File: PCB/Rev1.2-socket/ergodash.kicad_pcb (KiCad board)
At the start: 2 copper layers, 149.9 x 127.4 mm, 92 parts, among them J1 5PIN, M1 Speaker, SW1 SW_PUSH, SW10 SW_PUSH, SW11 SW_PUSH, SW12 SW_PUSH, SW13 SW_PUSH, SW14 SW_PUSH, SW15 SW_PUSH, SW16 SW_PUSH, SW17 SW_PUSH, SW18 SW_PUSH, SW19 SW_PUSH, SW2 SW_PUSH, SW20 SW_PUSH, SW21 SW_PUSH, SW22 SW_PUSH, SW23 SW_PUSH, SW24 SW_PUSH, SW25 SW_PUSH, SW26 SW_PUSH, SW27 SW_PUSH, SW28 SW_PUSH, SW29 SW_Push, SW3 SW_PUSH, SW30 SW_PUSH, SW31 SW_PUSH, SW32 SW_PUSH, SW33 SW_PUSH, SW34 SW_PUSH, SW35 SW_PUSH, SW36 SW_PUSH, SW37 SW_Push, SW38 SW_PUSH, SW39 SW_PUSH, SW4 SW_PUSH, SW40 SW_PUSH, SW41 SW_PUSH, SW5 SW_PUSH, SW6 SW_PUSH, SW7 SW_PUSH, SW8 SW_PUSH, SW9 SW_PUSH, U1 HOLE, U2 HOLE, U3 ProMicro, U4 HOLE, U5 HOLE, U7 HOLE, U8 HOLE, U9 HOLE

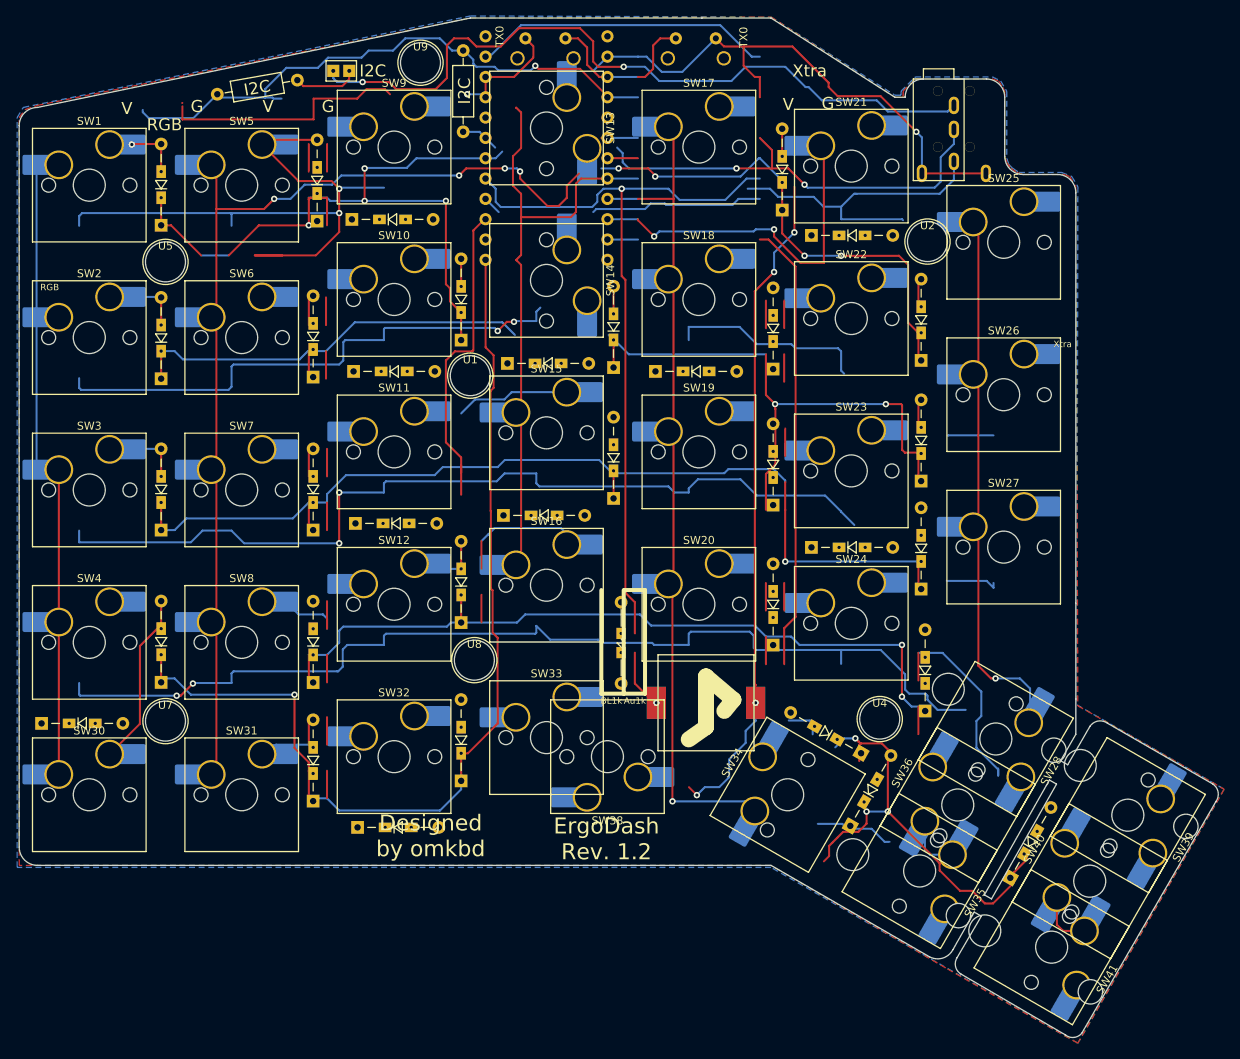
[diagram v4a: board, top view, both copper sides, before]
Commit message: Route the left board and drop alternative key layouts
Manual routing of the key matrix done in the GUI. Remove the
alternative-position switches (SW36, SW38, SW39, SW41) from the
schematic, keeping SW40 as the only 2U key, and delete the now
orphaned 2U stabilizer at the old SW36 position, which also
resolves the hole clearance conflict with the SW35 socket pad.
Re-apply the U6 on_board=no exclusion that was lost to a
concurrent eeschema save.

Co-Authored-By: Claude Fable 5 <noreply@anthropic.com>
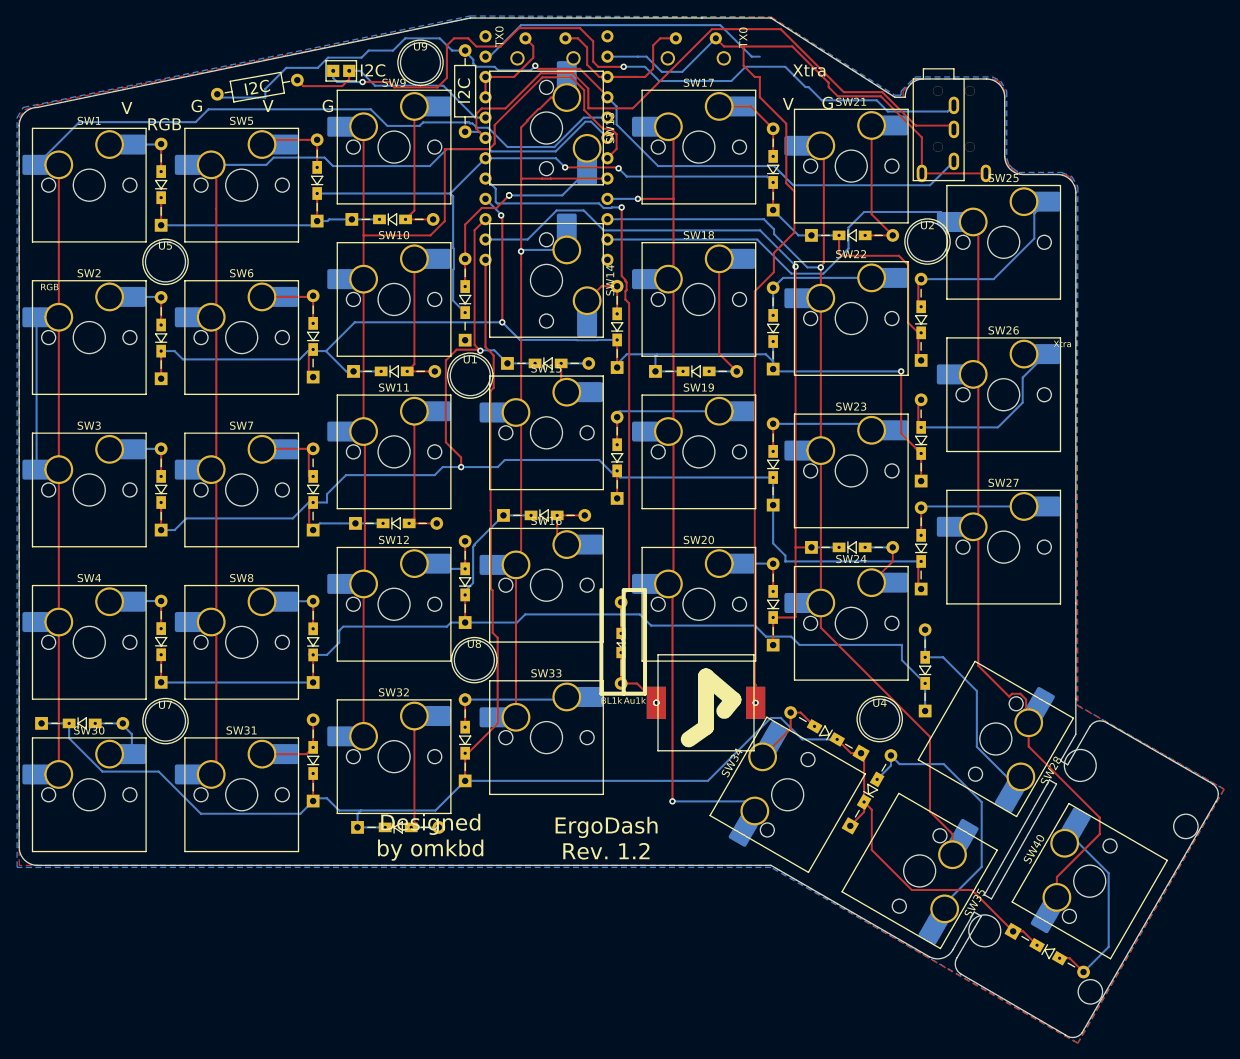
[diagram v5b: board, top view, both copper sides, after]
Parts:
- removed the ? at (195.6, 135.5)
- removed SW36, SW38, SW39, SW41: SW_PUSH, socket:SW_Hotswap_Kailh_MX_Plated
- moved D68 6.70 mm to (202.5, 151.3), turned to -30 degrees
- moved D17 1.13 mm to (172.5, 61.1)
- moved D13 0.50 mm to (134.0, 77.4)
- moved D12 0.50 mm to (134.0, 112.6)
- moved D32 0.50 mm to (134.0, 132.4)
- moved D14 0.45 mm to (153.0, 80.8)
- moved D19 0.45 mm to (153.0, 97.1)
- moved R2 0.25 mm to (134.0, 41.1)
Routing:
- net /col2: track 3.81 -> 130.9 mm
- net /col0: track 76.2 -> 173.3 mm
- net Net-(D18-A): track 112.7 -> 18.4 mm, vias 2 -> 0
- net /row1: track 246.0 -> 158.4 mm, vias 4 -> 3
- net /col5: track 52.7 -> 125.4 mm, vias 2 -> 1
- net Net-(D5-A): track 80.9 -> 10.6 mm, vias 2 -> 0
- net /col6: track 79.8 -> 146.1 mm, vias 1 -> 0
- net /row3: track 294.3 -> 231.8 mm, vias 4 -> 1
- net /row4: track 194.8 -> 235.9 mm, vias 4 -> 0
- net GND: track 198.4 -> 159.3 mm, vias 6 -> 1
- net Net-(D34-A): track 0.00 -> 32.7 mm
- net Net-(D68-A): track 0.00 -> 26.5 mm
- net /Audio: track 96.2 -> 73.7 mm
- net Net-(D13-A): track 3.45 -> 25.8 mm, vias 0 -> 2
- net Net-(D25-A): track 3.45 -> 24.9 mm
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
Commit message: Exclude SW37 (right-hand reset switch) from the left board
SW37 is the back-side reset switch used when the reversible board
served as the right half, so the left board does not need it.
Exclude it via on_board=no like U6 instead of moving it away from
the SW13 socket pad it overlapped. Also refill zones (clears stale
VCC fill under new row3 tracks) and document the thumb layout
decision in CLAUDE.md.

Co-Authored-By: Claude Fable 5 <noreply@anthropic.com>
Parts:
- removed SW37: SW_Push, library:tact_switch2
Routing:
- net /row0: track 148.4 -> 151.9 mm
- net /rst: track 24.6 -> 23.0 mm
- net GND: track 159.3 -> 157.9 mm
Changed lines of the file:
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@@
 		)
 	)
-	(footprint "library:tact_switch2"
-		(layer "B.Cu")
-		(at 144.018 39.624 180)
-		(property "Reference" "SW37"
-			(at 0 1.27 180)
-			(layer "Dwgs.User")
-			(hide yes)
-			(effects
-				(font
-					(size 1 1)
-					(thickness 0.15)
-				)
-			)
-		)
-		(property "Value" "SW_Push"
-			(at 0 -1.27 180)
-			(layer "B.Fab")
-			(effects
-				(font
-					(size 1 1)
-					(thickness 0.15)
-				)
-				(justify mirror)
-			)
-		)
-		(property "Datasheet" ""
-			(at 0 0 180)
-			(layer "F.Fab")
-			(hide yes)
-			(effects
-				(font
-					(size 1.27 1.27)
-				)
-			)
-		)
-		(property "Description" ""
-			(at 0 0 180)
-			(layer "F.Fab")
-			(hide yes)
-			(effects
-				(font
-					(size 1.27 1.27)
-				)
-			)
-		)
-		(sheetname "/")
-		(sheetfile "ergodash.kicad_sch")
-		(units
-			(unit
-				(name "A")
-				(pins "1" "2")
-			)
-		)
-		(attr through_hole)
-		(duplicate_pad_numbers_are_jumpers no)
-		(pad "1" thru_hole circle
-			(at -2.5 0 180)
-			(size 1.524 1.524)
-			(drill 0.762)
-			(layers "*.Cu" "*.Mask")
-			(remove_unused_layers no)
-			(net "/rst")
-			(pinfunction "1_1")
-			(pintype "passive")
-		)
-		(pad "2" thru_hole circle
-			(at 2.5 0 180)
-			(size 1.524 1.524)
-			(drill 0.762)
-			(layers "*.Cu" "*.Mask")
-			(remove_unused_layers no)
-			(net "GND")
-			(pinfunction "2_2")
-			(pintype "passive")
-		)
-		(pad "3" thru_hole circle
-			(at -3.5 -2.5 180)
-			(size 1.8 1.8)
-			(drill 1.3)
-			(layers "*.Cu" "*.Mask")
-			(remove_unused_layers no)
-		)
-		(pad "3" thru_hole circle
-			(at 3.5 -2.5 180)
-			(size 1.8 1.8)
-			(drill 1.3)
-			(layers "*.Cu" "*.Mask")
-			(remove_unused_layers no)
-		)
-		(embedded_fonts no)
-	)
 	(gr_line
 		(start 151.003 121.539)
@@
 	)
 	(segment
-		(start 148.082 39.624)
-		(end 146.518 39.624)
-		(width 0.254)
-		(layer "F.Cu")
-		(net "/rst")
-	)
-	(segment
 		(start 149.225 42.926)
 		(end 149.225 40.767)
@@
 	)
 	(segment
-		(start 142.494 40.6)
-		(end 141.518 39.624)
-		(width 0.254)
-		(layer "F.Cu")
-		(net "GND")
-	)
-	(segment
 		(start 140.081 44.45)
 		(end 136.525 44.45)
@@
 		(net "/row0")
 	)
+	(segment
+		(start 133.978 73.906)
+		(end 133.978 77.356)
+		(width 0.254)
+		(layer "F.Cu")
+		(net "/row0")
+	)
 	(via
 		(at 146.478 55.756)
@@
 	)
 	(segment
-		(start 131.699 113.157)
-		(end 132.207 112.649)
-		(width 0.254)
-		(layer "B.Cu")
-		(net "/row3")
-	)
-	(segment
-		(start 133.477 112.649)
-		(end 132.207 112.649)
-		(width 0.254)
-		(layer "B.Cu")
-		(net "/row3")
-	)
-	(segment
-		(start 118.237 115.168)
-		(end 116.713 116.692)
-		(width 0.254)
-		(layer "B.Cu")
-		(net "/row3")
-	)
-	(segment
-		(start 118.745 113.157)
-		(end 118.237 113.665)
-		(width 0.254)
-		(layer "B.Cu")
-		(net "/row3")
-	)
-	(segment
-		(start 118.237 113.665)
-		(end 118.237 115.168)
-		(width 0.254)
-		(layer "B.Cu")
-		(net "/row3")
-	)
-	(segment
-		(start 191.478 120.256)
-		(end 188.57601 117.35401)
-		(width 0.254)
-		(layer "B.Cu")
-		(net "/row3")
-	)
-	(segment
-		(start 116.713 116.692)
-		(end 114.448 116.692)
+		(start 172.501 115.443)
+		(end 172.478 115.466)
 		(width 0.254)
 		(layer "B.Cu")
@@
 	)
 	(segment
-		(start 114.448 116.692)
-		(end 114.427 116.671)
+		(start 188.57601 117.35401)
+		(end 188.57601 115.443)
 		(width 0.254)
 		(layer "B.Cu")
@@
 	)
 	(segment
-		(start 118.745 113.157)
-		(end 131.699 113.157)
+		(start 170.849 63.627)
+		(end 175.478 68.256)
 		(width 0.254)
 		(layer "B.Cu")
@@
 	)
 	(segment
-		(start 157.226 113.03)
-		(end 155.829 111.633)
+		(start 131.699 113.157)
+		(end 118.745 113.157)
 		(width 0.254)
 		(layer "B.Cu")
@@
 	)
 	(segment
-		(start 170.849 63.627)
-		(end 175.478 68.256)
+		(start 191.478 120.256)
+		(end 188.57601 117.35401)
 		(width 0.254)
 		(layer "B.Cu")
@@
 	(segment
 		(start 140.462 112.649)
-		(end 133.477 112.649)
+		(end 132.207 112.649)
 		(width 0.254)
 		(layer "B.Cu")
@@
 	)
 	(segment
-		(start 188.57601 115.443)
-		(end 175.768 115.443)
+		(start 118.745 113.157)
+		(end 118.237 113.665)
 		(width 0.254)
 		(layer "B.Cu")
@@
 	)
 	(segment
+		(start 132.207 112.649)
+		(end 131.699 113.157)
+		(width 0.254)
+		(layer "B.Cu")
+		(net "/row3")
+	)
+	(segment
 		(start 114.978 120.142)
 		(end 95.999 120.142)
@@
 	)
 	(segment
-		(start 171.577 114.406)
-		(end 170.201 113.03)
+		(start 188.57601 115.443)
+		(end 172.501 115.443)
 		(width 0.254)
 		(layer "B.Cu")
@@
 	)
 	(segment
-		(start 141.787454 64.77)
-		(end 145.416704 61.14075)
+		(start 157.226 113.03)
+		(end 155.829 111.633)
 		(width 0.254)
 		(layer "B.Cu")
@@
 	)
 	(segment
-		(start 170.201 113.03)
-		(end 157.226 113.03)
+		(start 141.787454 64.77)
+		(end 145.416704 61.14075)
 		(width 0.254)
 		(layer "B.Cu")
@@
 	)
 	(segment
-		(start 145.416704 61.14075)
-		(end 148.805303 61.14075)
+		(start 116.713 116.692)
+		(end 114.448 116.692)
 		(width 0.254)
 		(layer "B.Cu")
@@
 	)
 	(segment
-		(start 155.829 111.633)
-		(end 141.478 111.633)
+		(start 172.478 115.466)
+		(end 170.042 113.03)
+		(width 0.254)
+		(layer "B.Cu")
+		(net "/row3")
+	)
+	(segment
+		(start 145.416704 61.14075)
+		(end 148.805303 61.14075)
 		(width 0.254)
 		(layer "B.Cu")
@@
 	)
 	(segment
-		(start 188.57601 117.35401)
-		(end 188.57601 115.443)
+		(start 155.829 111.633)
+		(end 141.478 111.633)
+		(width 0.254)
+		(layer "B.Cu")
+		(net "/row3")
+	)
+	(segment
+		(start 118.237 115.168)
+		(end 116.713 116.692)
+		(width 0.254)
+		(layer "B.Cu")
+		(net "/row3")
+	)
+	(segment
+		(start 118.237 113.665)
+		(end 118.237 115.168)
 		(width 0.254)
 		(layer "B.Cu")
@@
 	)
 	(segment
-		(start 135.159 102.978187)
-		(end 134.978 103.159187)
+		(start 172.478 115.466)
+		(end 172.478 115.307)
 		(width 0.254)
 		(layer "B.Cu")
@@
 	)
 	(segment
-		(start 174.731 114.406)
-		(end 171.577 114.406)
+		(start 170.042 113.03)
+		(end 157.226 113.03)
 		(width 0.254)
 		(layer "B.Cu")
@@
 	)
 	(segment
-		(start 175.768 115.443)
-		(end 174.731 114.406)
+		(start 114.448 116.692)
+		(end 114.427 116.671)
+		(width 0.254)
+		(layer "B.Cu")
+		(net "/row3")
+	)
+	(segment
+		(start 135.159 102.978187)
+		(end 134.978 103.159187)
 		(width 0.254)
 		(layer "B.Cu")
